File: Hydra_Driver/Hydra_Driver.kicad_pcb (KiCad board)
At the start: 2 copper layers, 96 parts, among them IC1 ESP32-S3-WROOM-1-N4, IC2 DRV8313RHHR, IC3 DRV8313RHHR, J1 Conn_01x02, J2 Conn_01x02, J3 Conn_01x06, J4 Conn_01x06, J5 Conn_01x04, J6 Conn_01x04, J7 Conn_01x03, J8 Conn_01x03, J9 USB4105-GF-A, SW1 SW_SPST, SW2 SW_SPST, U1 MIC5365-3.3YC5, U2 USBLC6-2SC6, U3 74HC32, U4 INA199xxDCK, U5 INA199xxDCK, U6 74HC32, U7 INA199xxDCK, U8 INA199xxDCK

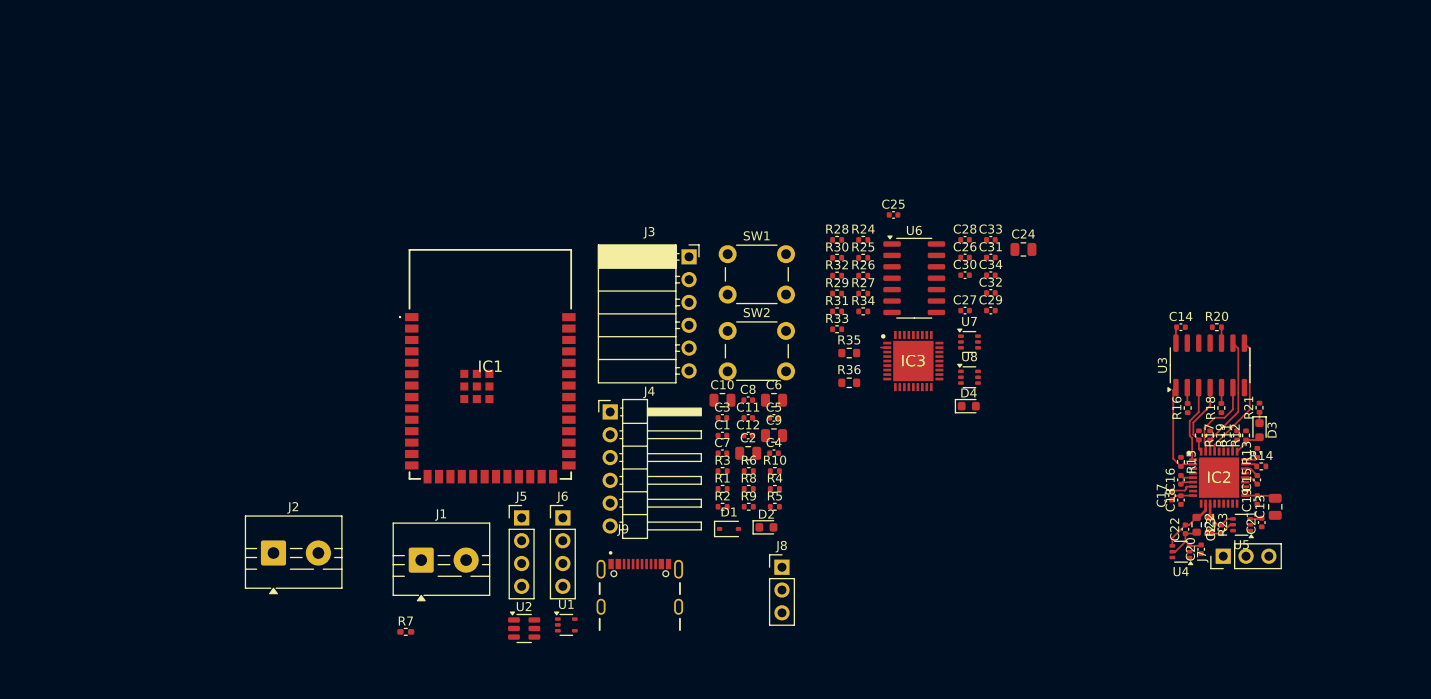
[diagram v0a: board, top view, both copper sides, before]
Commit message: Finished general layout of hydra board
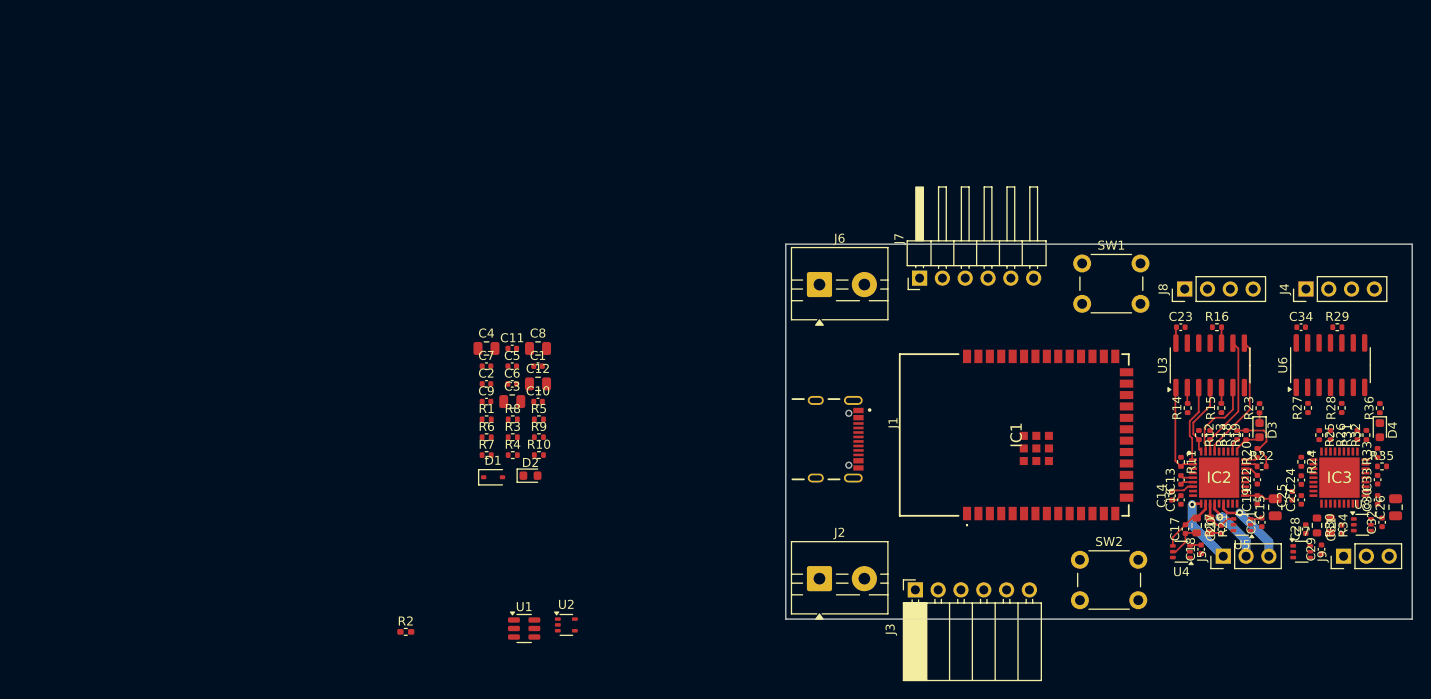
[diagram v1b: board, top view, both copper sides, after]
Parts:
- moved J4 91.0 mm to (143.2, 28.5), turned to 90 degrees
- moved J8 73.8 mm to (129.7, 28.5), turned to 90 degrees
- moved J6 67.7 mm to (89.0, 28.0)
- moved J9 62.5 mm to (147.4, 58.2), turned to 90 degrees
- moved R35 60.9 mm to (151.6, 48.2)
- moved R33 60.6 mm to (151.2, 46.8), turned to 90 degrees
- moved R32 59.4 mm to (149.9, 44.8), turned to 90 degrees
- moved R31 59.2 mm to (148.9, 44.8), turned to 90 degrees
- moved IC1 59.1 mm to (110.9, 44.8), turned to 90 degrees
- moved R36 58.5 mm to (151.4, 41.8), turned to 90 degrees
- moved R26 57.7 mm to (145.9, 44.8), turned to -90 degrees
- moved R24 57.3 mm to (142.7, 47.7), turned to -90 degrees
- moved R28 57.2 mm to (147.2, 41.7), turned to 90 degrees
- moved R25 57.2 mm to (144.7, 44.8), turned to -90 degrees
- moved R34 55.9 mm to (145.9, 54.8), turned to -90 degrees
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- renumbered C5 to C1, C4 to C10, C8 to C11, C9 to C12, C16 to C13, C17 to C14, C13 to C15, C18 to C16, C22 to C17, C20 to C18, C1 to C2, C23 to C20, C15 to C22, C14 to C23, C27 to C24, C28 to C25, C24 to C26, C29 to C27, C33 to C28, C31 to C29, C2 to C3, C34 to C31, C26 to C33, C25 to C34, C10 to C4, C11 to C5, C12 to C6, C3 to C7, C6 to C8, C7 to C9, J9 to J1, J1 to J2, J5 to J4, J7 to J5, J2 to J6, J4 to J7, J6 to J8, J8 to J9, R3 to R1, R5 to R10, R15 to R11, R17 to R12, R19 to R13, R16 to R14, R18 to R15, R20 to R16, R22 to R17, R11 to R18, R12 to R19, R7 to R2, R13 to R20, R23 to R21, R14 to R22, R21 to R23, R28 to R24, R30 to R25, R32 to R26, R29 to R27, R31 to R28, R33 to R29, R8 to R3, R35 to R30, R24 to R31, R25 to R32, R26 to R33, R36 to R34, R27 to R35, R34 to R36, R9 to R4, R10 to R5, R1 to R6, R2 to R7, R6 to R8, R4 to R9, U2 to U1, U1 to U2
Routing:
- net /OUT3A: track 0.00 -> 8.74 mm, vias 0 -> 1
- net +3.3V: track 6.15 -> 14.4 mm
- net /OUT1A: track 0.00 -> 8.22 mm, vias 0 -> 1
- net /OUT2A: track 0.00 -> 7.48 mm, vias 0 -> 1
- net GND: track 8.80 -> 5.38 mm
- net VMOT: track 6.02 -> 4.70 mm
- net /IN1HB: track 0.70 -> 0.00 mm
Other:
- board outline added: 69.8 x 41.8 mm

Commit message: Component placement mostly finalized
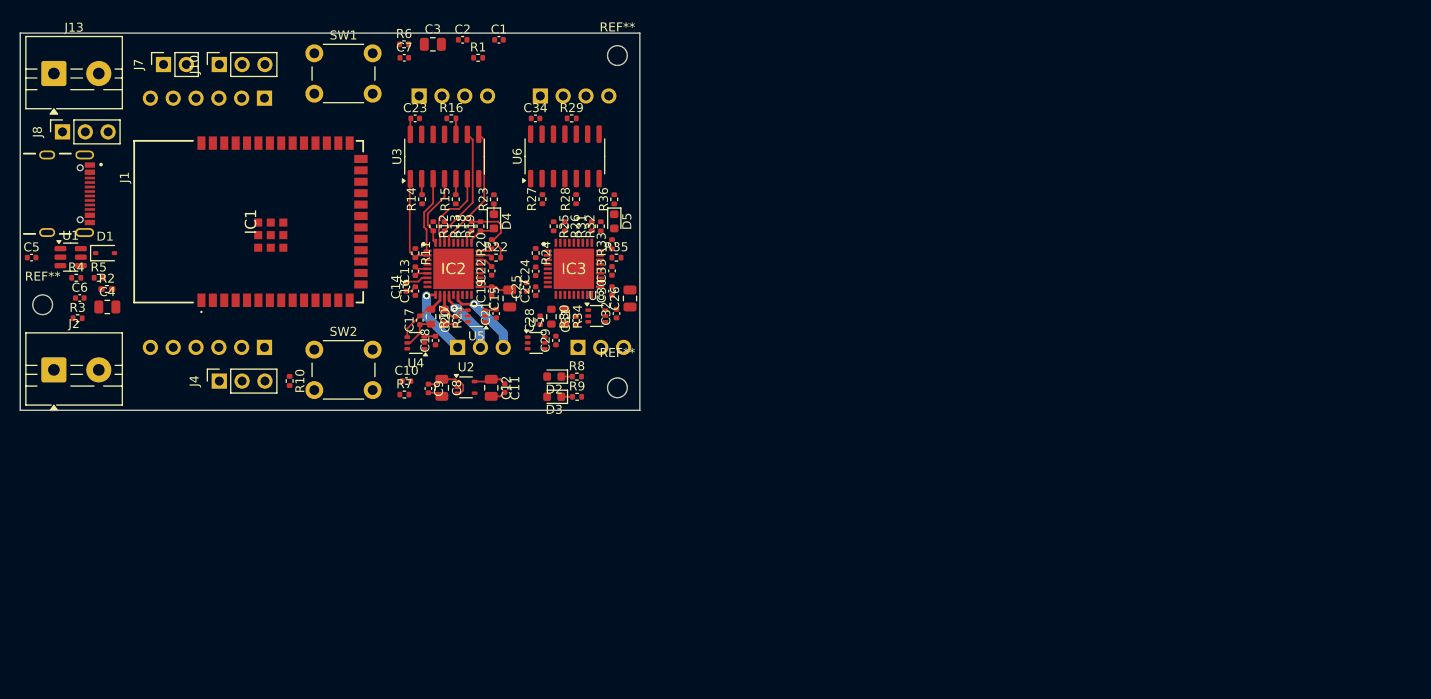
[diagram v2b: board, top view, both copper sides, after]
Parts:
- removed the R10 at (57.8, 47.0)
- added D3: LED, LED_SMD:LED_0603_1608Metric, F.Cu at (59.5, 40.5)
- added J10: Conn_01x03, Connector_PinSocket_2.54mm:PinSocket_1x03_P2.54mm_Vertical, F.Cu at (22.2, 3.50)
- added J4: Conn_01x03, Connector_PinSocket_2.54mm:PinSocket_1x03_P2.54mm_Vertical, F.Cu at (22.2, 38.8)
- added J7: Conn_01x02, Connector_PinSocket_2.54mm:PinSocket_1x02_P2.54mm_Vertical, F.Cu at (16.0, 3.50)
- added J8: Conn_01x03, Connector_PinSocket_2.54mm:PinSocket_1x03_P2.54mm_Vertical, F.Cu at (4.71, 11.0)
- added R9: 500, Resistor_SMD:R_0402_1005Metric, F.Cu at (62.0, 40.5)
- added REF**: MountingHole_2.2mm_M2, MountingHole:MountingHole_2.2mm_M2, F.Cu at (66.5, 2.50)
- added REF**: MountingHole_2.2mm_M2, MountingHole:MountingHole_2.2mm_M2, F.Cu at (2.50, 30.2)
- added REF**: MountingHole_2.2mm_M2, MountingHole:MountingHole_2.2mm_M2, F.Cu at (66.5, 39.5)
- J11: renamed from J8; moved to B.Cu
- J12: renamed from J9; moved to B.Cu
- J3: moved to B.Cu
- J5: renamed from J4; moved to B.Cu
- J6: renamed from J5; moved to B.Cu
- J9: renamed from J7; moved to B.Cu
- moved J1 89.8 mm to (3.00, 17.9)
- moved SW1 88.6 mm to (32.8, 2.25)
- moved IC1 88.5 mm to (25.7, 21.0)
- moved J13 88.4 mm to (3.75, 4.50)
- moved SW2 88.4 mm to (32.8, 35.2)
- moved J12 88.4 mm to (62.1, 35.0), turned to -90 degrees
- moved U4 88.4 mm to (44.0, 34.5)
- moved U5 88.4 mm to (50.8, 31.5)
- moved C13 88.4 mm to (44.0, 26.5)
- moved C14 88.4 mm to (43.0, 28.3)
- moved C15 88.4 mm to (54.5, 29.6)
- moved C16 88.4 mm to (44.0, 28.7)
- moved C17 88.4 mm to (44.5, 32.0)
- moved C18 88.4 mm to (46.2, 34.2)
- moved C19 88.4 mm to (52.5, 28.7)
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- renumbered D3 to D4, D4 to D5, J6 to J13, R9 to R10
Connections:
- IC1 pad 10: /SDA2 -> /SENSE2B
- IC1 pad 11: /SCL2 -> /IN1HA
- IC1 pad 12: /IN2HA -> unconnected-(IC1-IO8-Pad12)
- IC1 pad 15: /IN2LA -> /IN1LA
- IC1 pad 16: /IN3HA -> /IN2HA
- IC1 pad 17: /IN3LA -> /IN2LA
- IC1 pad 18: /IN1HB -> /IN3HA
- IC1 pad 19: /IN1LB -> /IN3LA
- IC1 pad 23: /IN2HB -> /IN1HB
- IC1 pad 24: /IN2LB -> /IN1LB
- IC1 pad 25: /IN3HB -> /IN2HB
- IC1 pad 26: /IN3LB -> /IN2LB
- IC1 pad 28: unconnected-(IC1-IO35-Pad28) -> /IN3HB
- IC1 pad 29: /SENSE1A -> /IN3LB
- IC1 pad 30: /SENSE2A -> /SDA1
- IC1 pad 31: unconnected-(IC1-IO38-Pad31) -> /SCL1
- IC1 pad 32: unconnected-(IC1-IO39-Pad32) -> /SDA2
- IC1 pad 33: unconnected-(IC1-IO40-Pad33) -> /SCL2
- IC1 pad 34: unconnected-(IC1-IO41-Pad34) -> /RESET
- IC1 pad 35: unconnected-(IC1-IO42-Pad35) -> /SLEEP
- IC1 pad 38: /SENSE2B -> /LED
- IC1 pad 4: /SENSE1B -> unconnected-(IC1-IO4-Pad4)
- IC1 pad 5: /SDA1 -> unconnected-(IC1-IO5-Pad5)
- IC1 pad 6: /SCL1 -> /SENSE1A
- IC1 pad 7: /IN1HA -> /SENSE2A
- IC1 pad 9: /IN1LA -> /SENSE1B
- J3 pad 1: +5V -> /CS
- J3 pad 2: GND -> /CLK
- J3 pad 3: /MOSI -> /LOOP1
- J3 pad 4: /LOOP -> /MOSI
- J3 pad 5: /CLK -> GND
- J3 pad 6: /CS -> +5V
- J9 pad 1: +5V -> /CS
- J9 pad 2: GND -> /CLK
- J9 pad 3: /MISO -> /LOOP2
- J9 pad 4: /LOOP -> /MISO
- J9 pad 5: /CLK -> GND
- J9 pad 6: /CS -> +5V
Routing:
- net +5V: track 0.00 -> 5.73 mm
- net +3.3V: track 14.4 -> 18.0 mm
- net GND: track 5.38 -> 8.72 mm
- net Net-(D3-K): track 0.00 -> 1.25 mm
- net Net-(D2-K): track 0.00 -> 1.23 mm
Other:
- board size 69.8 x 41.8 mm -> 69 x 42 mm

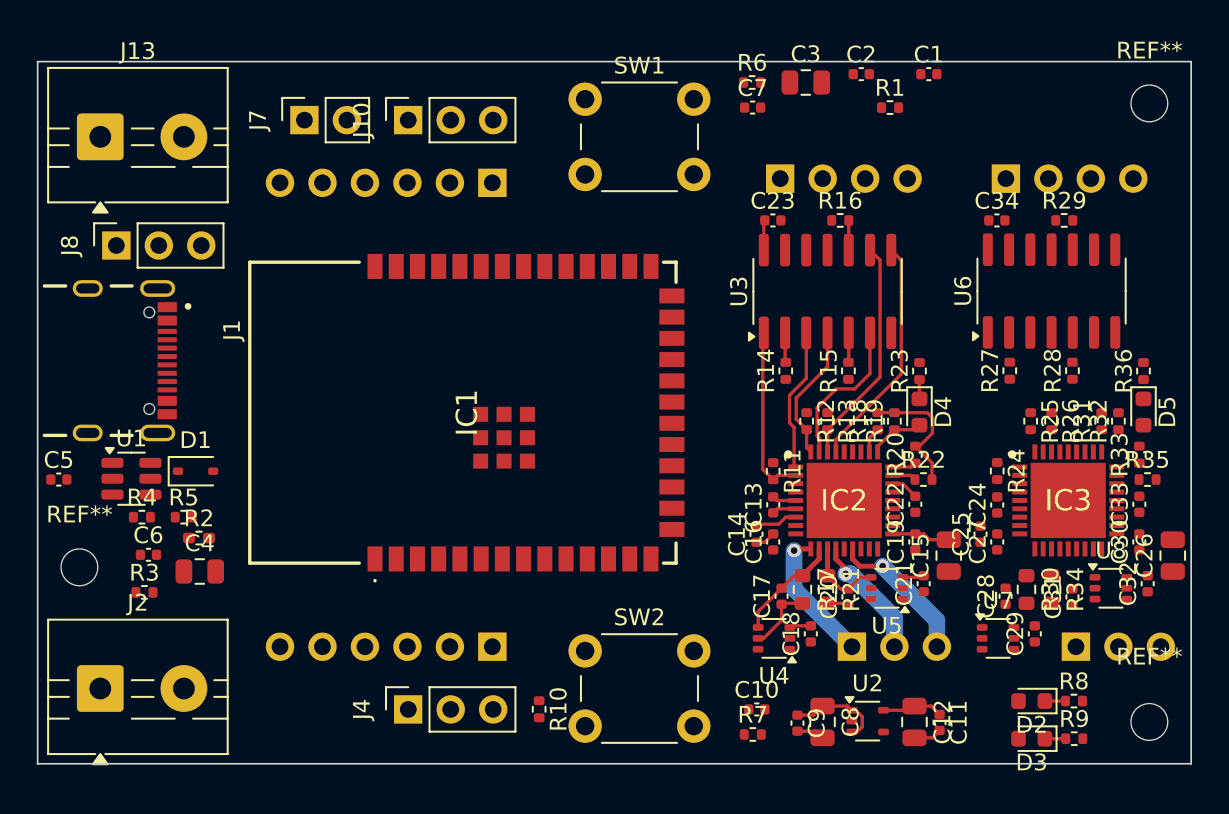
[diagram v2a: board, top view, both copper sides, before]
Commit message: Finished layout for main hydra board
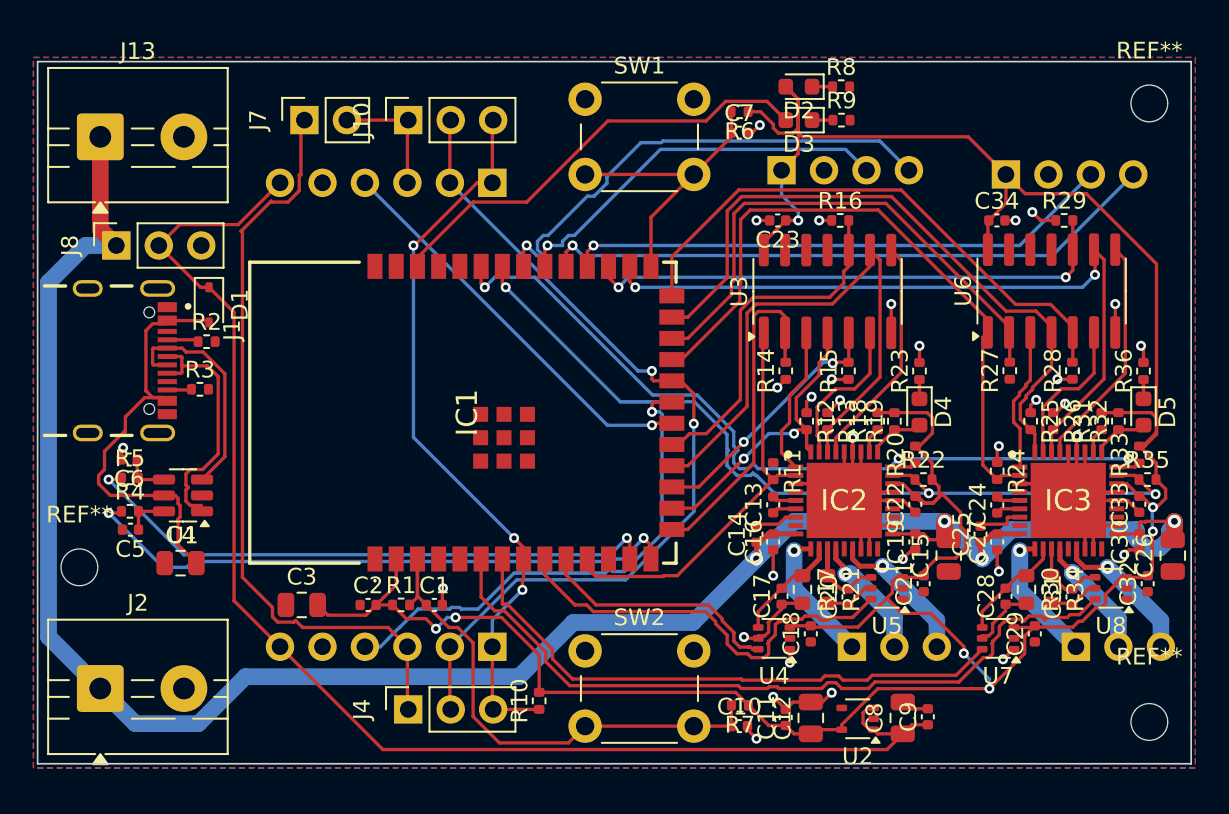
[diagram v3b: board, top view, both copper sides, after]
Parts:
- R2: footprint Resistor_SMD:R_0402_1005Metric_Pad0.72x0.64mm_HandSolder -> Resistor_SMD:R_0402_1005Metric
- moved C3 43.4 mm to (15.8, 32.5)
- moved C1 43.4 mm to (23.7, 32.5)
- moved C2 43.3 mm to (19.8, 32.5)
- moved R1 41.7 mm to (21.7, 32.5)
- moved D3 39.5 mm to (45.5, 3.50)
- moved R9 39.5 mm to (48.1, 3.50)
- moved D2 39.3 mm to (45.5, 1.50)
- moved R8 39.3 mm to (48.1, 1.50)
- moved R3 12.6 mm to (9.71, 19.6)
- moved R2 11.8 mm to (10.1, 16.8)
- moved D1 9.98 mm to (10.2, 14.6), turned to -90 degrees
- moved C11 9.20 mm to (44.8, 39.2), turned to 90 degrees
- moved C9 7.81 mm to (53.2, 39.2), turned to 90 degrees
- moved C12 6.20 mm to (46.2, 39.3), turned to 90 degrees
- moved C6 5.81 mm to (5.48, 23.8), turned to 180 degrees
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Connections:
- D3 pad 2: +3.3V -> /LED
- IC1 pad 10: /SENSE2B -> /SENSE1A
- IC1 pad 6: /SENSE1A -> /SENSE2B
- IC1 pad 7: /SENSE2A -> /SENSE1B
- IC1 pad 9: /SENSE1B -> /SENSE2A
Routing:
- net +3.3V: track 18.0 -> 185.1 mm, vias 0 -> 7
- net VMOT: track 4.70 -> 129.2 mm, vias 0 -> 4
- net GND: track 8.72 -> 105.7 mm, vias 0 -> 31
- net +5V: track 5.73 -> 82.0 mm
- net /CLK: track 0.00 -> 52.6 mm, vias 0 -> 2
- net /RESET: track 1.43 -> 52.0 mm, vias 0 -> 3
- net /SLEEP: track 1.45 -> 51.4 mm, vias 0 -> 3
- net /LOOP1: track 0.00 -> 45.5 mm
- net /SENSE2B: track 0.00 -> 45.4 mm
- net /IN3HB: track 0.00 -> 44.4 mm, vias 0 -> 2
- net /CS: track 0.00 -> 44.1 mm, vias 0 -> 3
- net /IN2HB: track 0.00 -> 39.9 mm
- net /IN1HB: track 0.00 -> 39.7 mm
- net /SCL1: track 0.00 -> 37.2 mm, vias 0 -> 1
- net /D+: track 0.00 -> 36.3 mm, vias 0 -> 2
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- added copper zone on B.Cu, net GND
- added copper zone on F.Cu, net GND

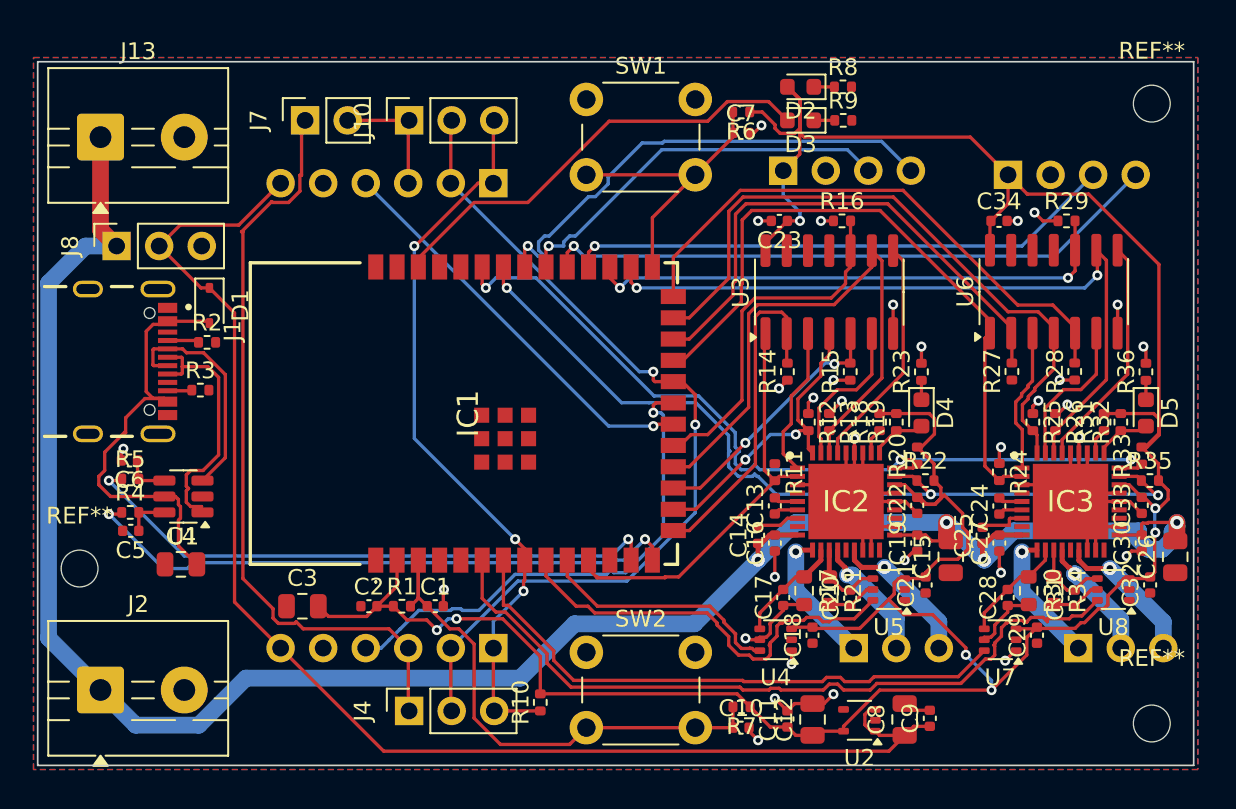
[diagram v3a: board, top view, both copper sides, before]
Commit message: Added silkscreen
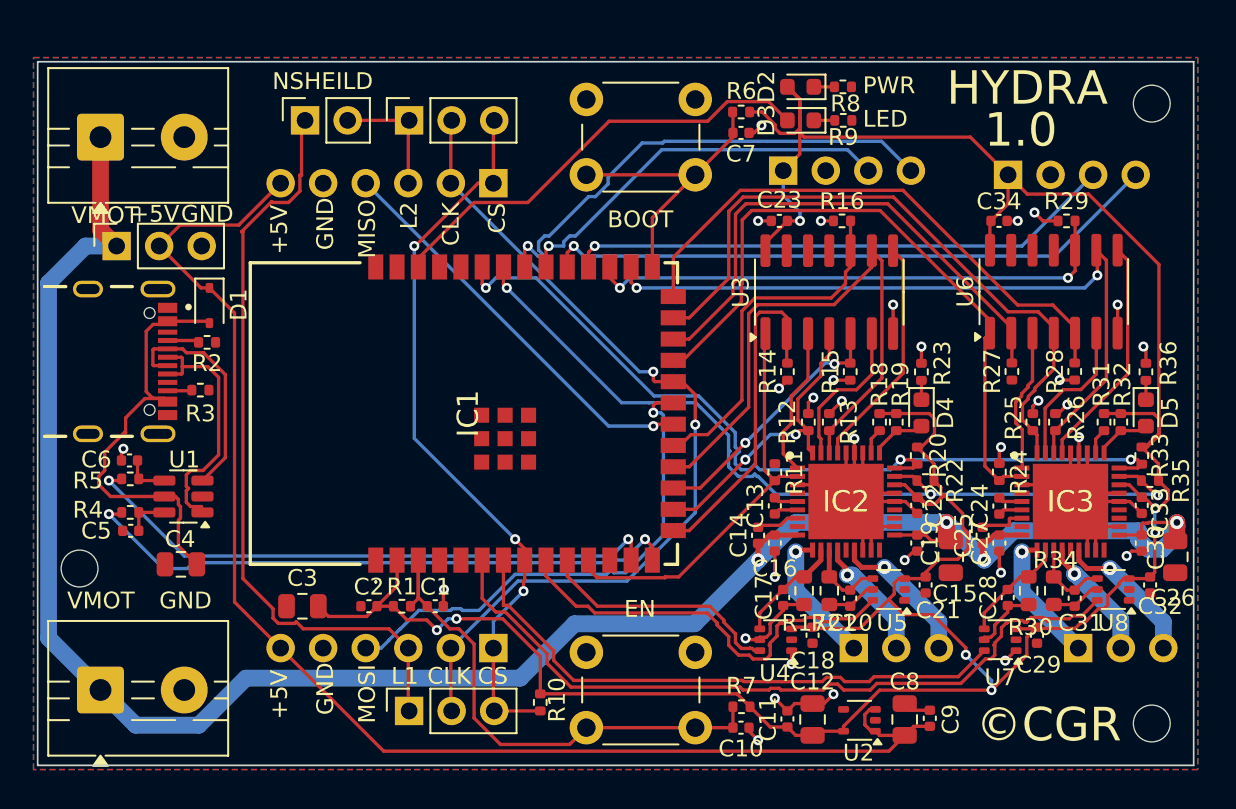
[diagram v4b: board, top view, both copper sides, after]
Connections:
- IC1 pad 30: /SDA1 -> /SDA2
- IC1 pad 31: /SCL1 -> /SCL2
- IC1 pad 32: /SDA2 -> /SDA1
- IC1 pad 33: /SCL2 -> /SCL1
- J11 pad 3: /SDA2 -> /SDA1
- J11 pad 4: /SCL2 -> /SCL1
- J5 pad 3: /SDA1 -> /SDA2
- J5 pad 4: /SCL1 -> /SCL2
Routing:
- net /SDA2: track 23.4 -> 32.9 mm
- net /SDA1: track 32.9 -> 23.4 mm
- net /SCL2: track 29.2 -> 37.2 mm
- net /SCL1: track 37.2 -> 29.2 mm
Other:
- board text added: "+3.3"
- board text added: "+5V"
- board text added: "1.0"
- board text added: "BOOT"
- board text added: "CLK"
- board text added: "CS"
- board text added: "EN"
- board text added: "GND"
- board text added: "HYDRA"
- board text added: "L1"
- board text added: "L2"
- board text added: "LED"
- board text added: "MISO"
- board text added: "MOSI"
- board text added: "MTRA"
- board text added: "MTRB"
- board text added: "NSHEILD"
- board text added: "PWR"
- board text added: "SCL1"
- board text added: "SCL2"
- board text added: "SDA1"
- board text added: "SDA2"
- board text added: "VMOT"
- board text added: "©CGR"
